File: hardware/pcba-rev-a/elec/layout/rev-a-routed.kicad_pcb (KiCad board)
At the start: 2 copper layers, 200 x 175 mm, 180 parts

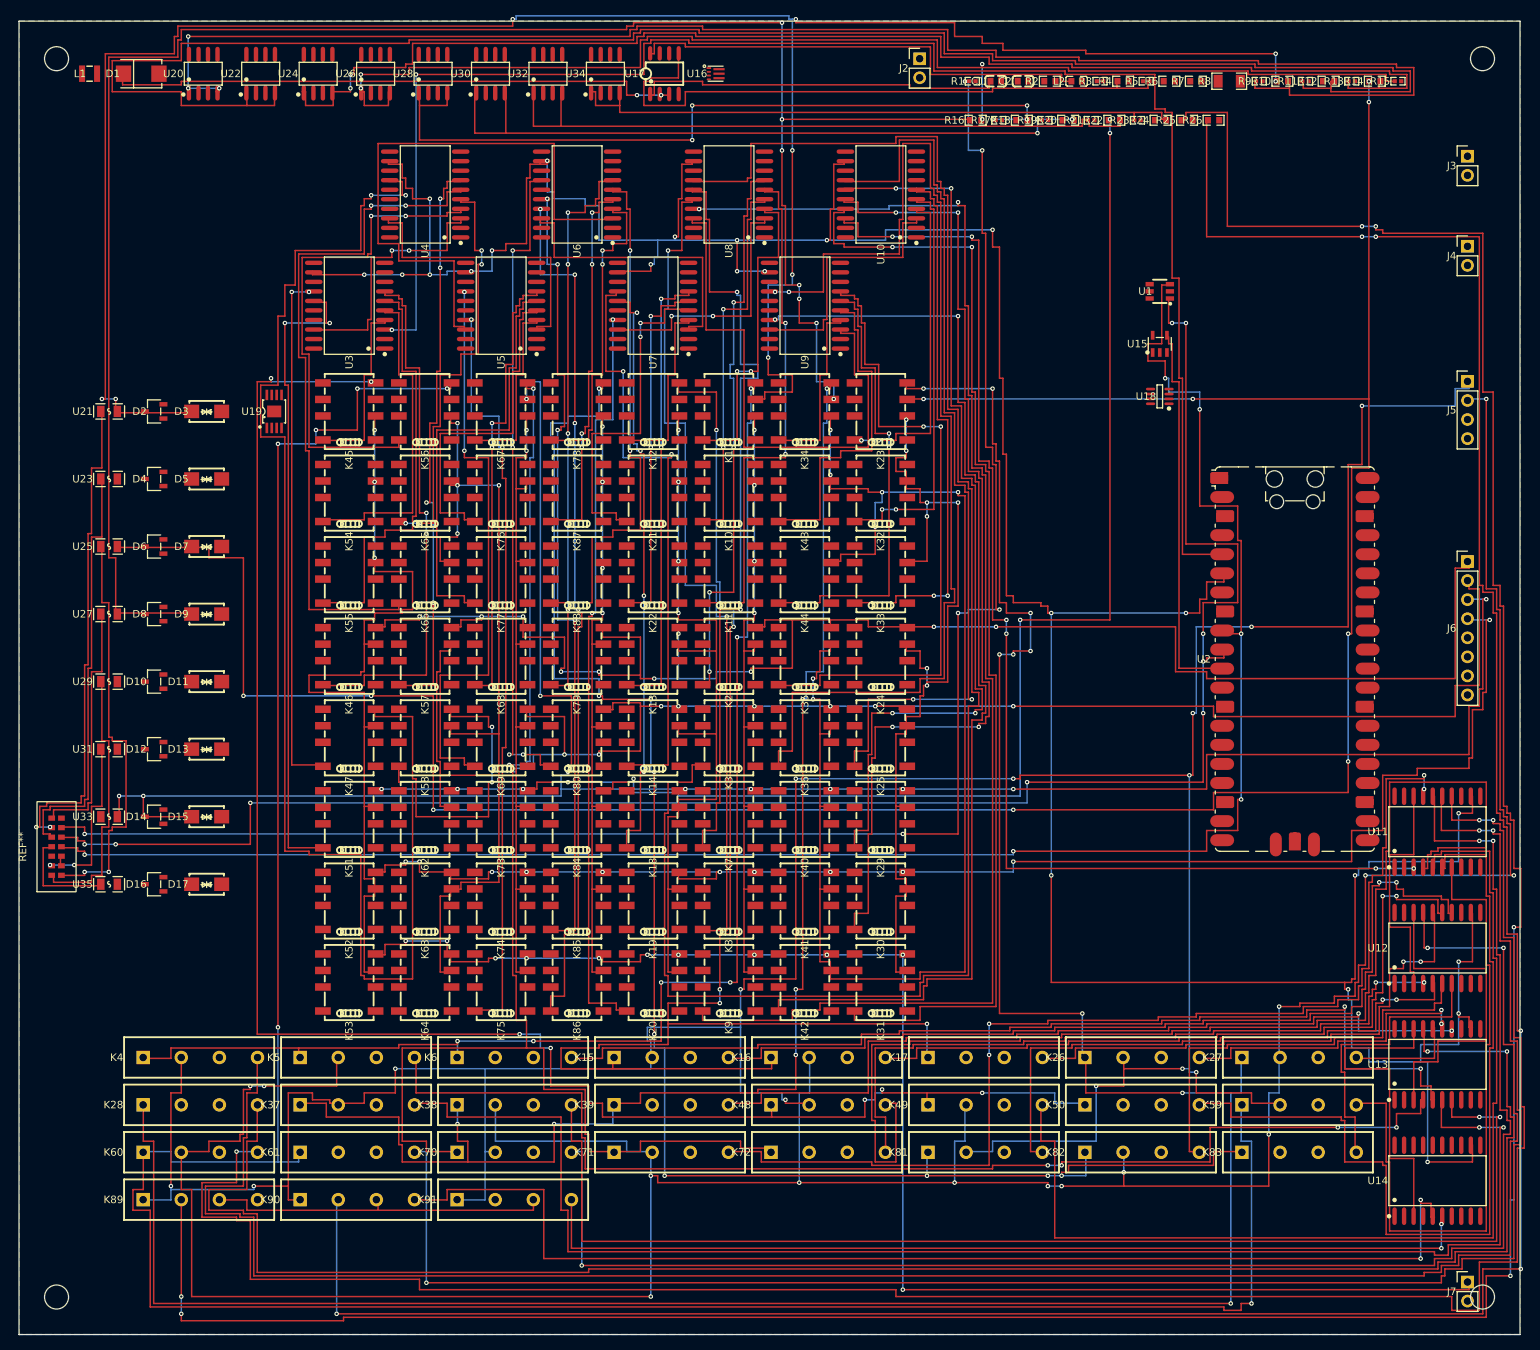
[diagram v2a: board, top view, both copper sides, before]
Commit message: flroute v1: 100% first-pass routing (174/174) on FL-1 Rev A
PathFinder negotiated congestion + four structural mechanisms that close
the last mile a congestion model can't express:

- Fanout escape stubs: fine-pitch pads (0.5mm VSON / 0.65mm MSOP) walled
  in by neighbor clearance halos at cell granularity get exact-coordinate
  escape wires, legality-checked against true pad boxes, iterated to
  fixpoint with an orphan veto for nearby pins.
- Hard consolidation ordered by pin-pocket tightness (tightest first).
- Transactional rip-and-swap with iterative deepening: pocket BFS with
  pads AND copper as walls, via-legal layer hops, foreign via centers
  and ring-blocking tracks attributed as rippable sealers; rollback on
  failure keeps the routed total monotone.
- Emission: pad-shape-aware terminal snapping (circle pads have no
  copper in bbox corners), tree junctions never moved, unused stubs
  dropped.

Also: board was declared 2-layer — In1/In2 zones were orphaned and KiCad
exported a 2-layer DSN. SetCopperLayerCount(4) in place_and_zone.py
(150 -> 169 routed from that fix alone).

Benchmark (Rev A, 174 signal nets): flroute v1 174/174 routed, all
signal nets connected, 2 minor clearance defects (0.16 vs 0.20mm),
~170s headless. freerouting 1.9: ~93%, 7 copper defects, ~16min, GUI.
Remaining unconnected items are zone-rail stitching vias (pipeline
scope, import_route.py).

Co-Authored-By: Claude Fable 5 <noreply@anthropic.com>
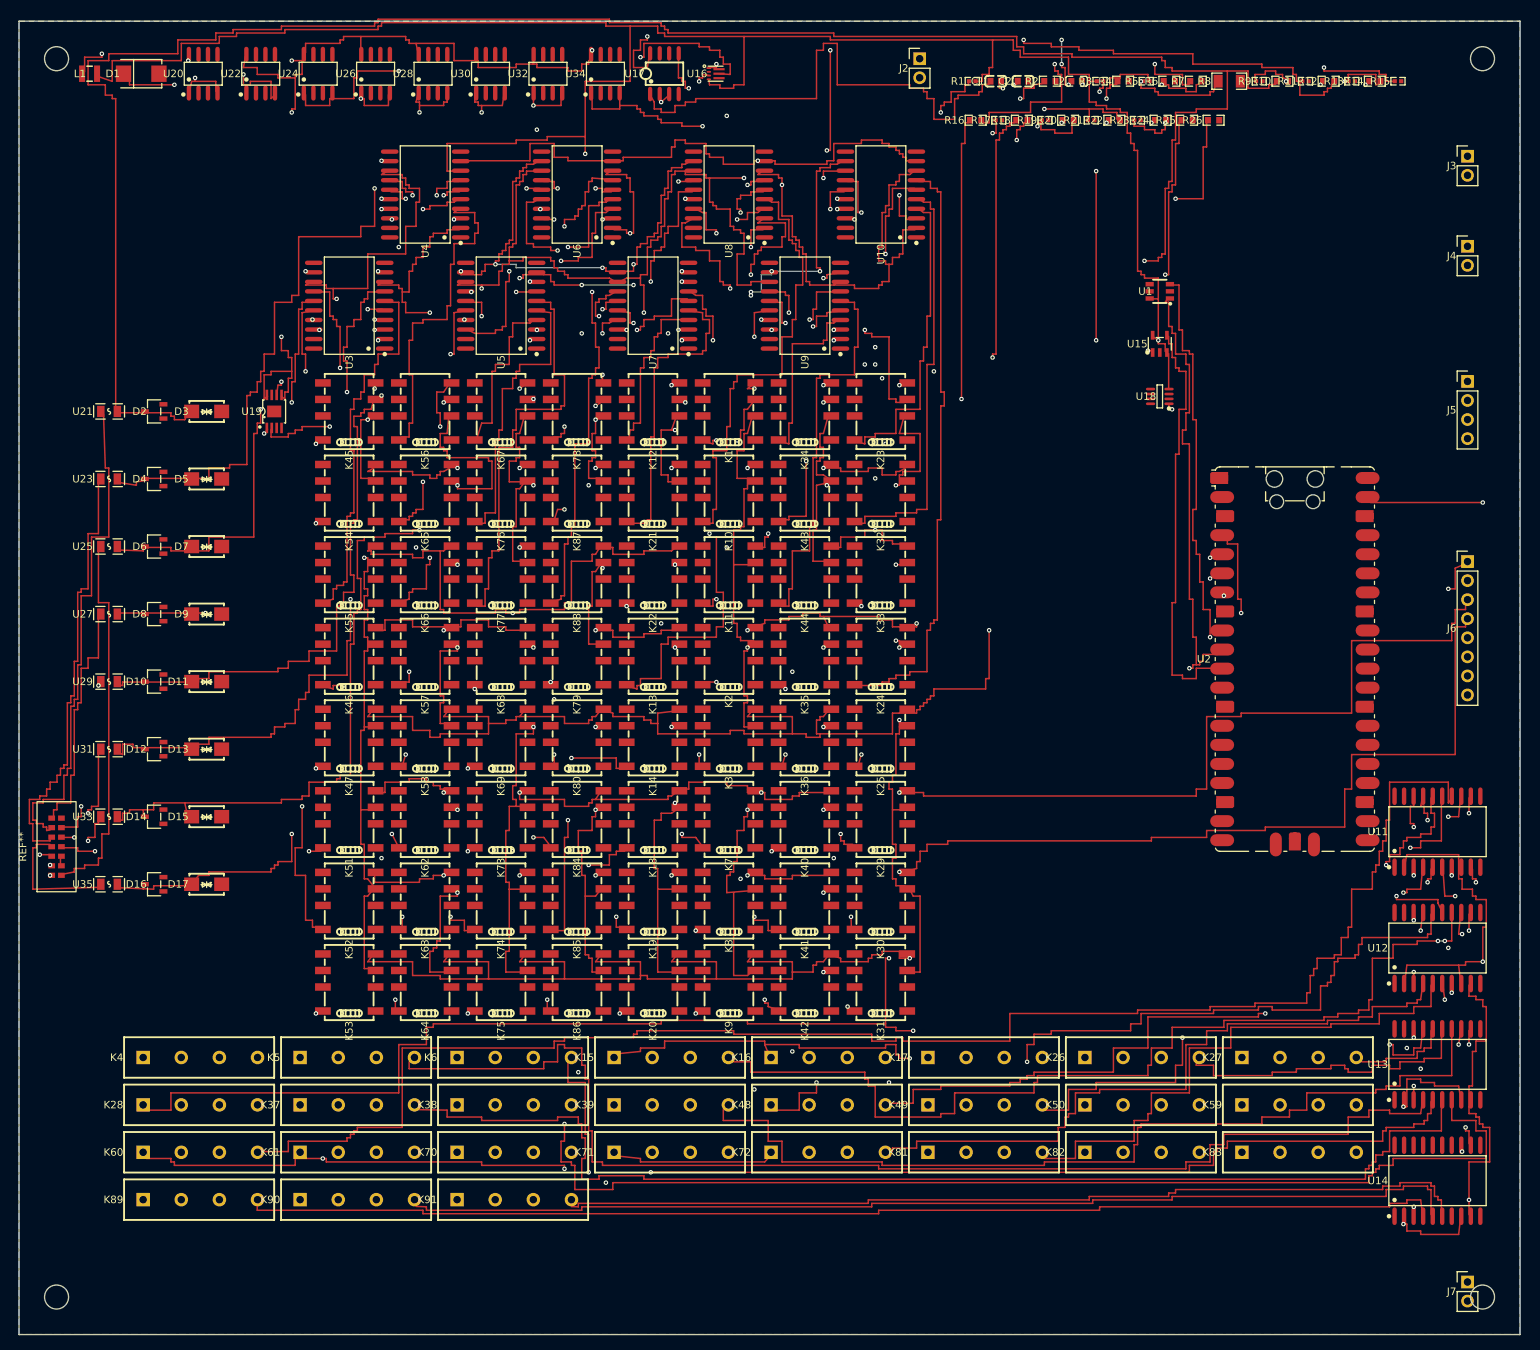
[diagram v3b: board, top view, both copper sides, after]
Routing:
- net hv: track 0.00 -> 804.2 mm, vias 0 -> 16
- net nG: track 0.00 -> 457.8 mm, vias 0 -> 12
- net SRCK: track 0.00 -> 432.1 mm, vias 0 -> 11
- net scope_b: track 0.00 -> 255.4 mm, vias 0 -> 4
- net node-7: track 0.00 -> 249.8 mm, vias 0 -> 6
- net node-1: track 0.00 -> 247.1 mm, vias 0 -> 3
- net EN: track 0.00 -> 242.5 mm, vias 0 -> 5
- net v3v3-hv: track 0.00 -> 223.0 mm, vias 0 -> 6
- net node-5: track 0.00 -> 213.0 mm, vias 0 -> 3
- net scope_a: track 0.00 -> 203.4 mm, vias 0 -> 6
- net node-4: track 0.00 -> 195.7 mm, vias 0 -> 3
- net power-FB: track 0.00 -> 175.4 mm, vias 0 -> 2
- net sink_1k: track 0.00 -> 159.7 mm
- net coil_n-18: track 236.4 -> 87.8 mm, vias 0 -> 2
- net c_nr-power-hv: track 0.00 -> 139.8 mm, vias 0 -> 3
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- added copper zone on In1.Cu, net lv
- added copper zone on In2.Cu, net sel_p4-coil_bus-hv
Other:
- copper layers 2 -> 4

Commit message: Zone-rail stitching: 136/145 plane pads connected, 0 new DRC defects
flroute skips the two zone-served nets (lv, coil rail) since the pours carry
them, but the pours are on inner/bottom layers while the nets' 145 SMD pads
are on F.Cu — each needs a stitching via down to its plane.

scripts/stitch_vias.py, two tiers:
- via-in-pad (76): a same-net via fully inside the host pad merges on F.Cu and
  adds no copper, so it cannot create a new F.Cu clearance defect — but a
  THROUGH via still punches In1/In2/B.Cu and must clear other-net copper there
  (the first cut checked only F.Cu and shorted to inner routing: 109 shorts).
  Off-center in-pad search dodges inner-layer tracks running under the pad.
- fanout (60): standard via in the nearest open spot, joined by a short
  collision-checked F.Cu stub; spiral search to 3mm, 15deg, two stub widths.

All vias honor board rules: >=0.5/0.3mm via/drill, 0.5mm edge clearance,
0.25mm hole-to-hole, layer-aware clearance via KiCad effective-shape
collision. Zone fill clearance dropped 0.5->0.25mm (lv) / 0.3mm (hv coil),
still above the 0.2mm rule, so planes flood through track gaps and reconnect
dead islands.

zone-net unconnected 157 -> 24; DRC delta vs baseline = 0 on every type.
Residual 24 is structural (In1/In2 are both routing and plane layers): 9 IC
power/GND pins boxed in on all 4 layers + ~15 island-stranded. Root cause and
three fix options documented in docs/zone-stitching.md (EVT call: hand-finish
the 9 pins).

Co-Authored-By: Claude Opus 4.8 (1M context) <noreply@anthropic.com>
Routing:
- net lv: track 0.00 -> 39.8 mm, vias 0 -> 71
- net sel_p4-coil_bus-hv: track 0.00 -> 29.6 mm, vias 0 -> 65
